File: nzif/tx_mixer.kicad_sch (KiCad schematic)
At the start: 28 parts, among them U1 SN74CBT3125CPW, U2 SN74CBT3125CPW, U3 SN74CBT3125CPW

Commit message: cartoons on main2
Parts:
- gave numbers to parts that had none: 3
- renumbered C2 to C282, C4 to C283, C5 to C284, C6 to C285, C11 to C286, C12 to C287, C13 to C288, C14 to C289, C1 to C290, C3 to C291, C7 to C292, C8 to C293, C15 to C294, C16 to C295, C17 to C296, C18 to C297, C9 to C299, C19 to C300, C20 to C301, C10 to C303, C21 to C304, C22 to C305, U1 to U136, U2 to U137, U3 to U138
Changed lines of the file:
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@@
 		(dnp no)
 		(fields_autoplaced yes)
-		(property "Reference" "C?"
+		(property "Reference" "C302"
 			(at 104.14 38.0935 0)
 			(effects
@@
 		(dnp no)
 		(fields_autoplaced yes)
-		(property "Reference" "C21"
+		(property "Reference" "C304"
 			(at 226.06 36.8235 0)
 			(effects
@@
 		(dnp no)
 		(fields_autoplaced yes)
-		(property "Reference" "C14"
+		(property "Reference" "C289"
 			(at 213.3536 134.62 90)
 			(effects
@@
 		(dnp no)
 		(fields_autoplaced yes)
-		(property "Reference" "#PWR05"
+		(property "Reference" "#PWR0305"
 			(at 219.71 110.49 0)
 			(effects
@@
 		(dnp no)
 		(fields_autoplaced yes)
-		(property "Reference" "C13"
+		(property "Reference" "C288"
 			(at 213.3536 119.38 90)
 			(effects
@@
 		(dnp no)
 		(fields_autoplaced yes)
-		(property "Reference" "#PWR?"
+		(property "Reference" "#PWR0306"
 			(at 106.68 48.26 0)
 			(effects
@@
 		(dnp no)
 		(fields_autoplaced yes)
-		(property "Reference" "C22"
+		(property "Reference" "C305"
 			(at 226.06 100.3235 0)
 			(effects
@@
 		(dnp no)
 		(fields_autoplaced yes)
-		(property "Reference" "#PWR022"
+		(property "Reference" "#PWR?"
 			(at 81.28 99.06 0)
 			(effects
@@
 				)
 			)
+			(project "nzif"
+				(path "/fe42ca2f-2bb8-4d5a-9e84-807788ed632f/2802166e-37f5-44e9-af25-f372a0fd0bf8"
+					(reference "#PWR?")
+					(unit 1)
+				)
+			)
 		)
 	)
@@
 		(dnp no)
 		(fields_autoplaced yes)
-		(property "Reference" "#PWR021"
+		(property "Reference" "#PWR?"
 			(at 80.01 35.56 0)
 			(effects
@@
 				)
 			)
+			(project "nzif"
+				(path "/fe42ca2f-2bb8-4d5a-9e84-807788ed632f/2802166e-37f5-44e9-af25-f372a0fd0bf8"
+					(reference "#PWR?")
+					(unit 1)
+				)
+			)
 		)
 	)
@@
 		(dnp no)
 		(fields_autoplaced yes)
-		(property "Reference" "C9"
+		(property "Reference" "C299"
 			(at 95.25 101.5935 0)
 			(effects
@@
 		(dnp no)
 		(fields_autoplaced yes)
-		(property "Reference" "#PWR?"
+		(property "Reference" "#PWR0310"
 			(at 116.84 92.71 0)
 			(effects
@@
 		(dnp no)
 		(fields_autoplaced yes)
-		(property "Reference" "C19"
+		(property "Reference" "C300"
 			(at 217.17 36.8235 0)
 			(effects
@@
 		(dnp no)
 		(fields_autoplaced yes)
-		(property "Reference" "C7"
+		(property "Reference" "C292"
 			(at 95.2436 113.03 90)
 			(effects
@@
 		(on_board yes)
 		(dnp no)
-		(property "Reference" "U2"
+		(property "Reference" "U137"
 			(at 257.556 42.418 0)
 			(effects
@@
 		(dnp no)
 		(fields_autoplaced yes)
-		(property "Reference" "C6"
+		(property "Reference" "C285"
 			(at 91.4336 135.89 90)
 			(effects
@@
 		(dnp no)
 		(fields_autoplaced yes)
-		(property "Reference" "#PWR02"
+		(property "Reference" "#PWR0307"
 			(at 106.68 111.76 0)
 			(effects
@@
 		(dnp no)
 		(fields_autoplaced yes)
-		(property "Reference" "C1"
+		(property "Reference" "C290"
 			(at 95.2436 49.53 90)
 			(effects
@@
 		(on_board yes)
 		(dnp no)
-		(property "Reference" "#PWR03"
+		(property "Reference" "#PWR0311"
 			(at 116.84 156.21 0)
 			(effects
@@
 		(on_board yes)
 		(dnp no)
-		(property "Reference" "U?"
+		(property "Reference" "U135"
 			(at 135.636 43.688 0)
 			(effects
@@
 		(dnp no)
 		(fields_autoplaced yes)
-		(property "Reference" "C10"
+		(property "Reference" "C303"
 			(at 104.14 101.5935 0)
 			(effects
@@
 		(dnp no)
 		(fields_autoplaced yes)
-		(property "Reference" "#PWR04"
+		(property "Reference" "#PWR0304"
 			(at 219.71 46.99 0)
 			(effects
@@
 		(dnp no)
 		(fields_autoplaced yes)
-		(property "Reference" "C4"
+		(property "Reference" "C283"
 			(at 91.4336 72.39 90)
 			(effects
@@
 		(dnp no)
 		(fields_autoplaced yes)
-		(property "Reference" "C20"
+		(property "Reference" "C301"
 			(at 217.17 100.3235 0)
 			(effects
@@
 		(dnp no)
 		(fields_autoplaced yes)
-		(property "Reference" "#PWR07"
+		(property "Reference" "#PWR0309"
 			(at 228.6 110.49 0)
 			(effects
@@
 		(dnp no)
 		(fields_autoplaced yes)
-		(property "Reference" "C15"
+		(property "Reference" "C294"
 			(at 217.1636 48.26 90)
 			(effects
@@
 		(dnp no)
 		(fields_autoplaced yes)
-		(property "Reference" "C16"
+		(property "Reference" "C295"
 			(at 217.1636 63.5 90)
 			(effects
@@
 		(on_board yes)
 		(dnp no)
-		(property "Reference" "U3"
+		(property "Reference" "U138"
 			(at 257.556 105.918 0)
 			(effects
@@
 		(dnp no)
 		(fields_autoplaced yes)
-		(property "Reference" "#PWR01"
+		(property "Reference" "#PWR0303"
 			(at 97.79 111.76 0)
 			(effects
@@
 		(dnp no)
 		(fields_autoplaced yes)
-		(property "Reference" "C11"
+		(property "Reference" "C286"
 			(at 213.3536 55.88 90)
 			(effects
@@
 		(dnp no)
 		(fields_autoplaced yes)
-		(property "Reference" "C18"
+		(property "Reference" "C297"
 			(at 217.1636 127 90)
 			(effects
@@
 		(on_board yes)
 		(dnp no)
-		(property "Reference" "U1"
+		(property "Reference" "U136"
 			(at 135.636 107.188 0)
 			(effects
@@
 		(dnp no)
 		(fields_autoplaced yes)
-		(property "Reference" "C12"
+		(property "Reference" "C287"
 			(at 213.3536 71.12 90)
 			(effects
@@
 		(dnp no)
 		(fields_autoplaced yes)
-		(property "Reference" "#PWR?"
+		(property "Reference" "#PWR0302"
 			(at 97.79 48.26 0)
 			(effects
@@
 		(dnp no)
 		(fields_autoplaced yes)
-		(property "Reference" "C8"
+		(property "Reference" "C293"
 			(at 95.2436 128.27 90)
 			(effects
@@
 		(dnp no)
 		(fields_autoplaced yes)
-		(property "Reference" "#PWR08"
+		(property "Reference" "#PWR0312"
 			(at 238.76 91.44 0)
 			(effects
@@
 		(dnp no)
 		(fields_autoplaced yes)
-		(property "Reference" "C17"
+		(property "Reference" "C296"
 			(at 217.1636 111.76 90)
 			(effects
@@
 		(dnp no)
 		(fields_autoplaced yes)
-		(property "Reference" "#PWR09"
+		(property "Reference" "#PWR0313"
 			(at 238.76 154.94 0)
 			(effects
@@
 		(dnp no)
 		(fields_autoplaced yes)
-		(property "Reference" "#PWR024"
+		(property "Reference" "#PWR?"
 			(at 201.93 97.79 0)
 			(effects
@@
 				)
 			)
+			(project "nzif"
+				(path "/fe42ca2f-2bb8-4d5a-9e84-807788ed632f/2802166e-37f5-44e9-af25-f372a0fd0bf8"
+					(reference "#PWR?")
+					(unit 1)
+				)
+			)
 		)
 	)
@@
 		(dnp no)
 		(fields_autoplaced yes)
-		(property "Reference" "C2"
+		(property "Reference" "C282"
 			(at 91.4336 57.15 90)
 			(effects
@@
 		(dnp no)
 		(fields_autoplaced yes)
-		(property "Reference" "#PWR06"
+		(property "Reference" "#PWR0308"
 			(at 228.6 46.99 0)
 			(effects
@@
 		(dnp no)
 		(fields_autoplaced yes)
-		(property "Reference" "C3"
+		(property "Reference" "C291"
 			(at 95.2436 64.77 90)
 			(effects
@@
 		(dnp no)
 		(fields_autoplaced yes)
-		(property "Reference" "C?"
+		(property "Reference" "C298"
 			(at 95.25 38.0935 0)
 			(effects
@@
 		(dnp no)
 		(fields_autoplaced yes)
-		(property "Reference" "#PWR023"
+		(property "Reference" "#PWR?"
 			(at 203.2 34.29 0)
 			(effects
@@
 				)
 			)
+			(project "nzif"
+				(path "/fe42ca2f-2bb8-4d5a-9e84-807788ed632f/2802166e-37f5-44e9-af25-f372a0fd0bf8"
+					(reference "#PWR?")
+					(unit 1)
+				)
+			)
 		)
 	)
@@
 		(dnp no)
 		(fields_autoplaced yes)
-		(property "Reference" "C5"
+		(property "Reference" "C284"
 			(at 91.4336 120.65 90)
 			(effects

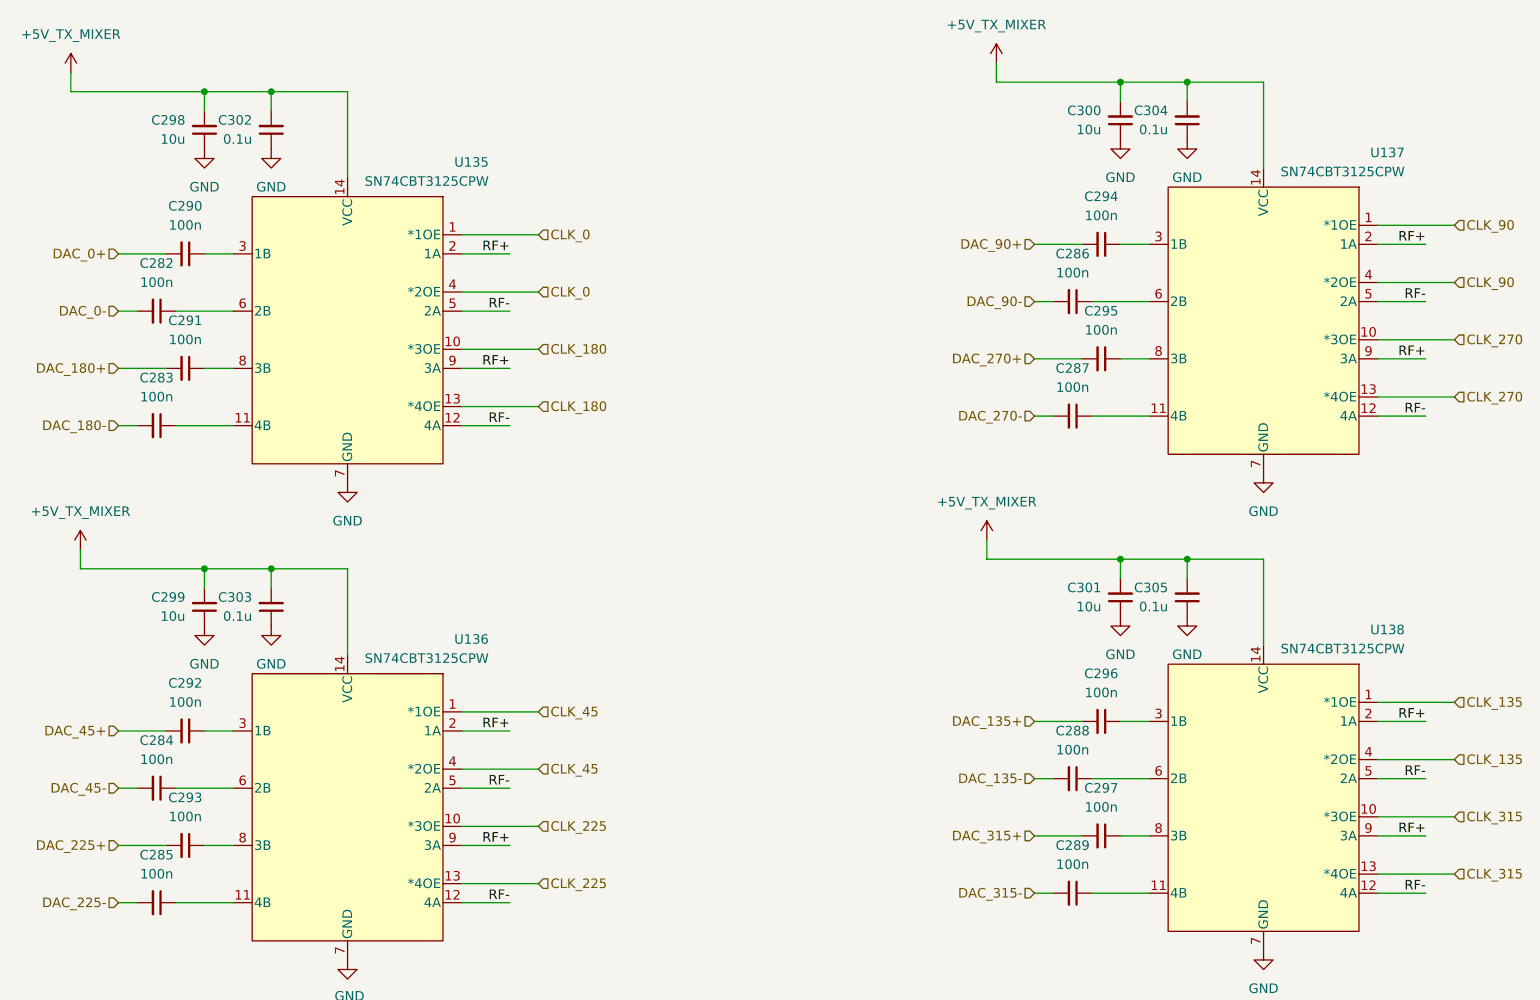
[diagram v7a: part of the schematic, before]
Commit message: wire top sheet from rf front end through rx driver amps
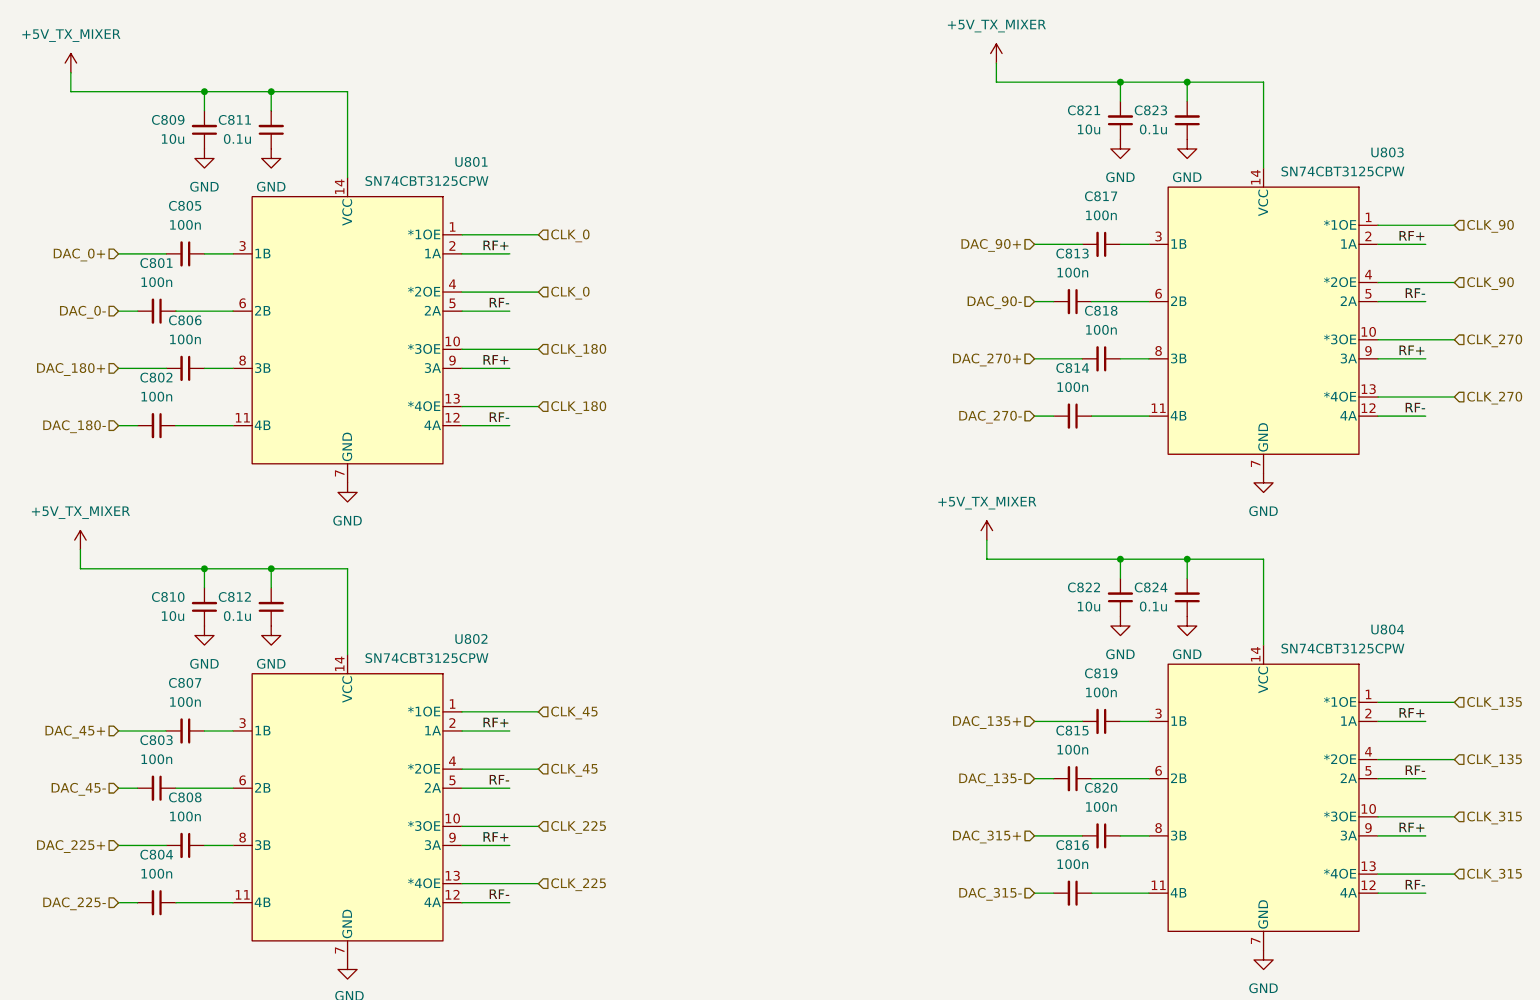
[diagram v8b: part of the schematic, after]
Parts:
- renumbered C282 to C801, C283 to C802, C284 to C803, C285 to C804, C290 to C805, C291 to C806, C292 to C807, C293 to C808, C298 to C809, C299 to C810, C302 to C811, C303 to C812, C286 to C813, C287 to C814, C288 to C815, C289 to C816, C294 to C817, C295 to C818, C296 to C819, C297 to C820, C300 to C821, C301 to C822, C304 to C823, C305 to C824, U135 to U801, U136 to U802, U137 to U803, U138 to U804
